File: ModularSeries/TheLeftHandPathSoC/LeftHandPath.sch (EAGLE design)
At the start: 64 parts, among them IC3 556_DUALTIMERDIL14, Q1 2N3906, Q2 2N3904, Q3 2N3904

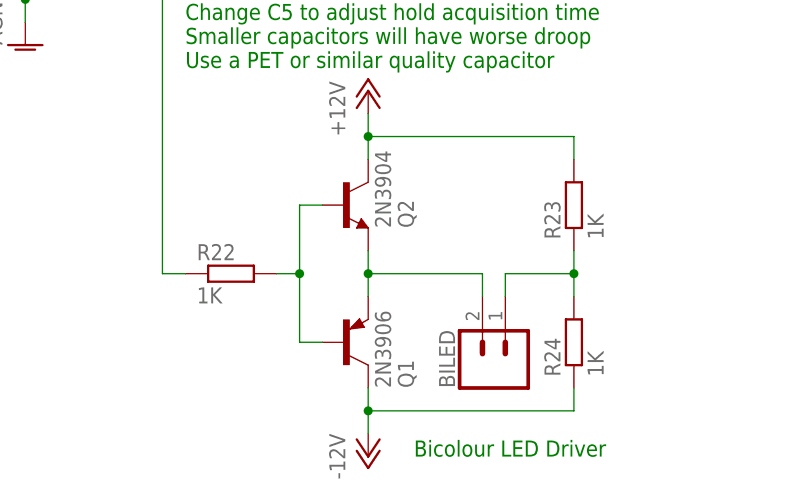
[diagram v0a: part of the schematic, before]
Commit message: Portals schematic renders brought up to date
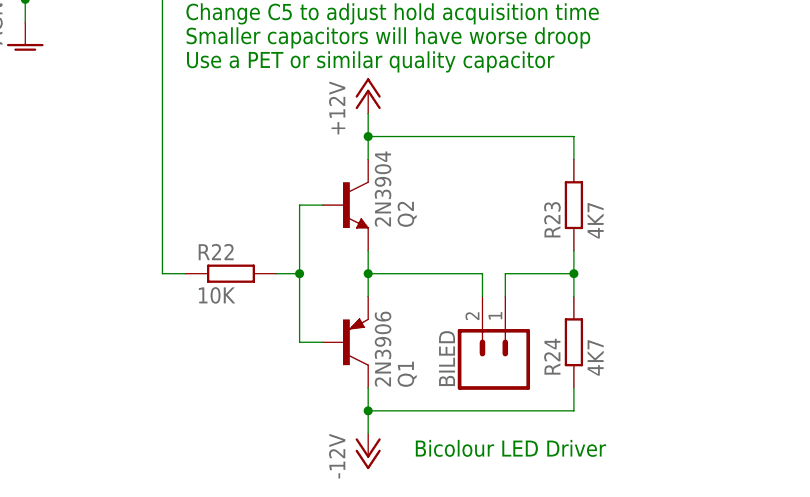
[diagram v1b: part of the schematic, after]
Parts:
- R22: value 1K -> 10K
- R23, R24: value 1K -> 4K7
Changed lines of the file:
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@@
 <part name="R21" library="rcl" library_urn="urn:adsk.eagle:library:334" deviceset="R-EU_" device="0207/7" package3d_urn="urn:adsk.eagle:package:23493/2" value="100Ω"/>
 <part name="WP1" library="ElectricNoodleBox" deviceset="COMBO_SUPPLY_HEADER" device=""/>
-<part name="R22" library="rcl" library_urn="urn:adsk.eagle:library:334" deviceset="R-EU_" device="0207/7" package3d_urn="urn:adsk.eagle:package:23493/2" value="1K"/>
+<part name="R22" library="rcl" library_urn="urn:adsk.eagle:library:334" deviceset="R-EU_" device="0207/7" package3d_urn="urn:adsk.eagle:package:23493/2" value="10K"/>
 <part name="Q2" library="transistor" library_urn="urn:adsk.eagle:library:402" deviceset="2N3904" device="" package3d_urn="urn:adsk.eagle:package:28523/2"/>
 <part name="Q1" library="transistor-pnp" library_urn="urn:adsk.eagle:library:399" deviceset="2N3906" device="" package3d_urn="urn:adsk.eagle:package:29211/2"/>
 <part name="P+4" library="supply1" library_urn="urn:adsk.eagle:library:371" deviceset="+12V" device=""/>
 <part name="P-3" library="supply1" library_urn="urn:adsk.eagle:library:371" deviceset="-12V" device=""/>
-<part name="R23" library="rcl" library_urn="urn:adsk.eagle:library:334" deviceset="R-EU_" device="0207/7" package3d_urn="urn:adsk.eagle:package:23493/2" value="1K"/>
-<part name="R24" library="rcl" library_urn="urn:adsk.eagle:library:334" deviceset="R-EU_" device="0207/7" package3d_urn="urn:adsk.eagle:package:23493/2" value="1K"/>
+<part name="R23" library="rcl" library_urn="urn:adsk.eagle:library:334" deviceset="R-EU_" device="0207/7" package3d_urn="urn:adsk.eagle:package:23493/2" value="4K7"/>
+<part name="R24" library="rcl" library_urn="urn:adsk.eagle:library:334" deviceset="R-EU_" device="0207/7" package3d_urn="urn:adsk.eagle:package:23493/2" value="4K7"/>
 <part name="BILED" library="ElectricNoodleBox" deviceset="2XWIREPAD" device=""/>
 </parts>

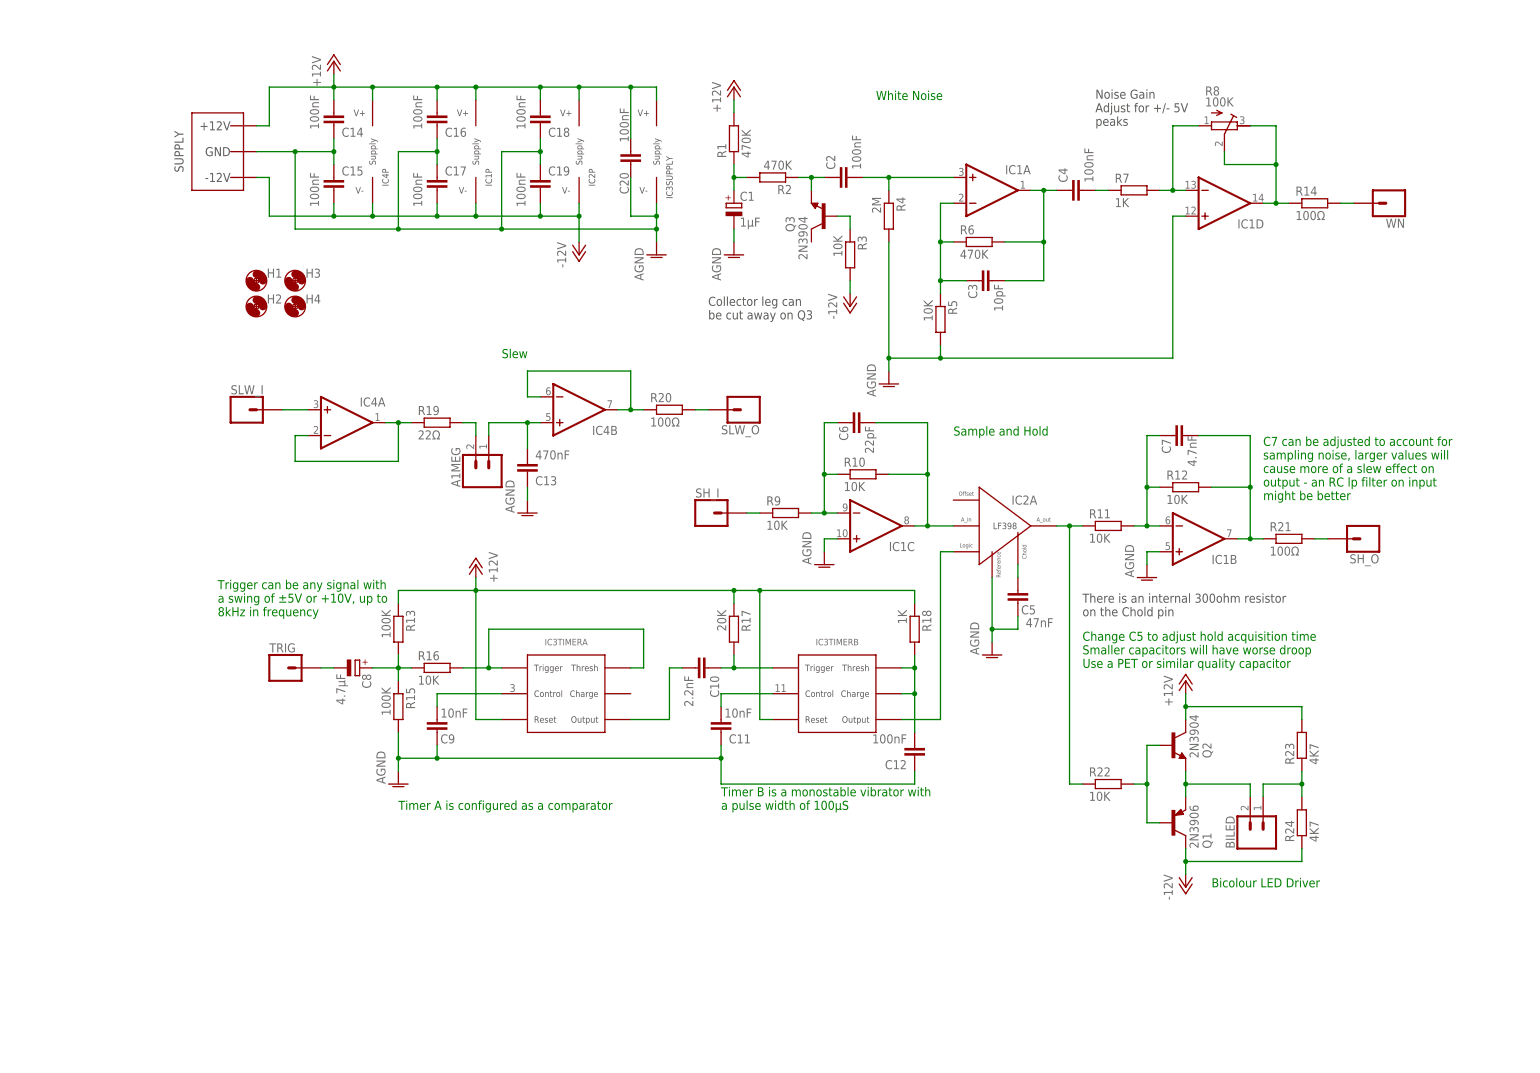
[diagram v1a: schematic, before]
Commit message: Left Hand Path Project added, Core, Control and Panel Cards
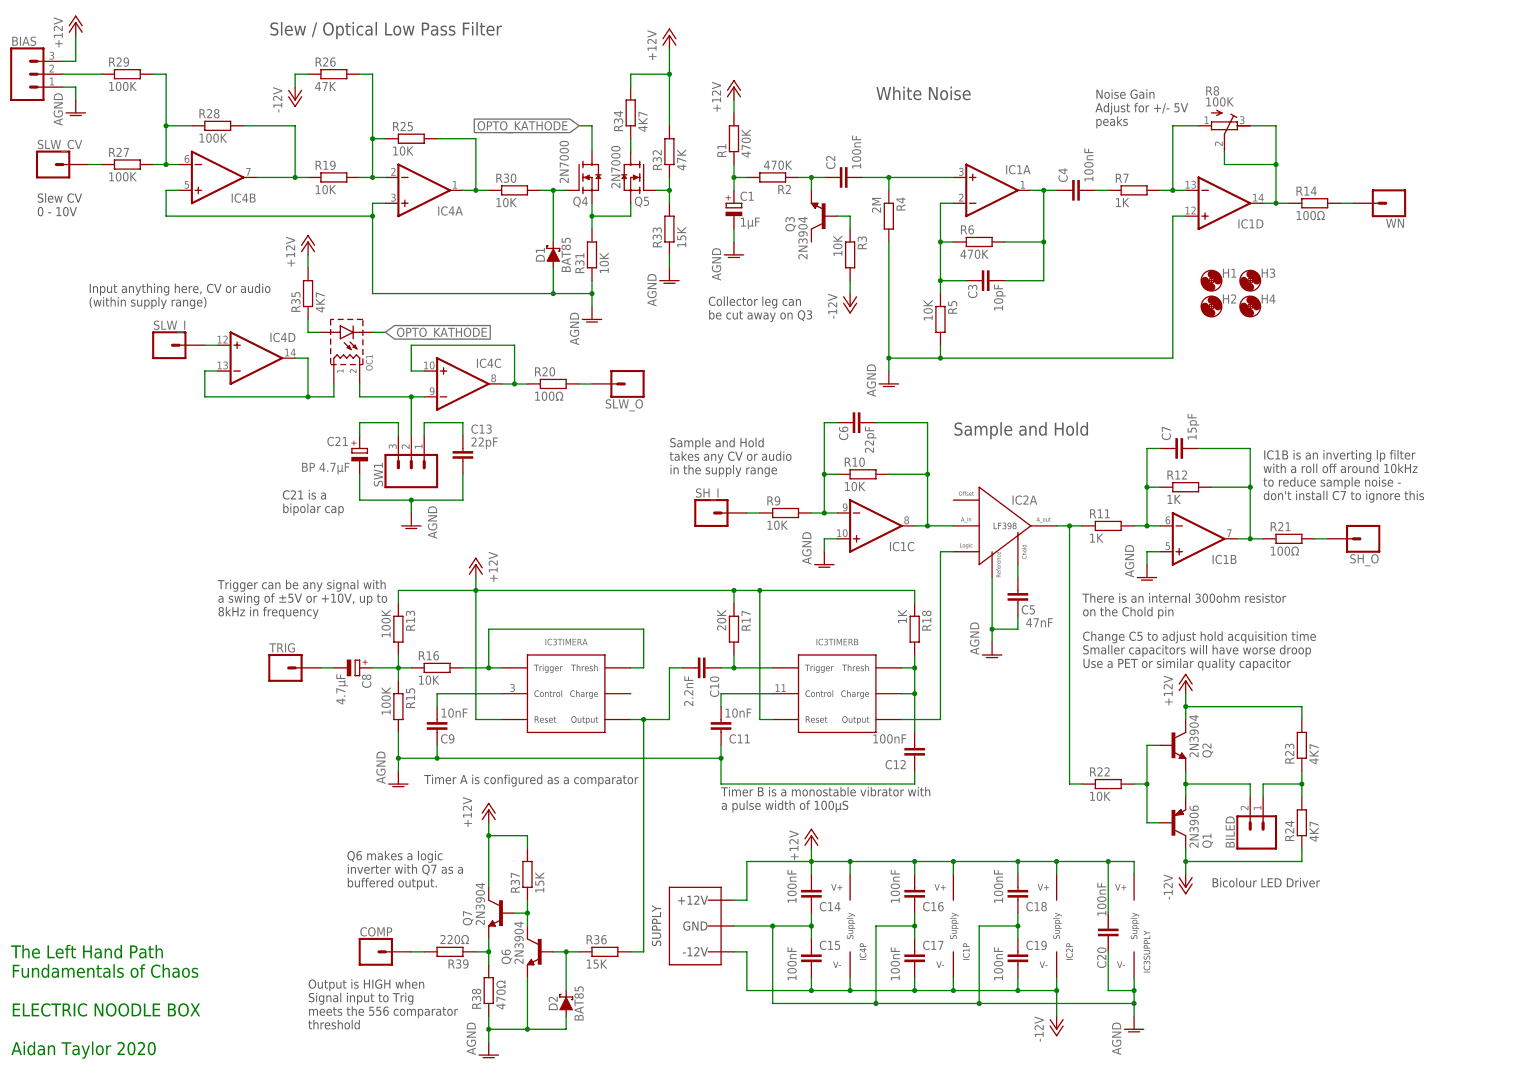
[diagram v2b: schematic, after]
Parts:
- removed A1MEG: 2XWIREPAD, ElectricNoodleBox:2XWIREPAD
- added BIAS, SW1: 3XWIREPAD, ElectricNoodleBox:3XWIREPAD
- added C21: BP 4.7µF, rcl:CPOL-EUE2-5
- added COMP, SLW_CV: 1XWIREPAD, ElectricNoodleBox:1XWIREPAD
- added D1, D2: BAT85, ElectricNoodleBox:SCHOTTKY_DO35
- added OC1: OPTOCOUPLERSILONEX, ElectricNoodleBox:OPTOCOUPLERSILONEX
- added Q4, Q5: 2N7000, ElectricNoodleBox:2N7000
- added Q6, Q7: 2N3904, transistor:2N3904
- added R25, R30, R31: 10K, rcl:R-EU_0207/7
- added R26, R32: 47K, rcl:R-EU_0207/7
- added R27, R28, R29: 100K, rcl:R-EU_0207/7
- added R33, R36, R37: 15K, rcl:R-EU_0207/7
- added R34, R35: 4K7, rcl:R-EU_0207/7
- added R38: 470Ω, rcl:R-EU_0207/7
- added R39: 220Ω, rcl:R-EU_0207/7
- C13: value 470nF -> 22pF
- C7: value 4.7nF -> 15pF
- IC4: device ElectricNoodleBox:TL0X2DIL -> ElectricNoodleBox:TL0X4DIL
- R11, R12: value 10K -> 1K
- R19: value 22Ω -> 10K
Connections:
- new net N$37: IC4A.-IN, R19.2, R25.1, R26.2
- new net N$38: IC4B.-IN, R27.2, R28.1, R29.2
- new net N$39: IC4A.OUT, R25.2, R30.1
- new net N$40: D1.C, Q4.G, R30.2
- new net N$41: Q4.S, Q5.S, R31.2
- new net N$42: C21.+, SW1.3
- new net N$43: Q5.G, R32.1, R33.2
- new net N$44: Q5.D, R34.1
- new net N$45: OC1.A, R35.1
- new net N$46: C13.2, SW1.1
- new net N$47: R27.1, SLW_CV.1
- new net N$48: BIAS.2, R29.1
- new net N$49: Q6.C, Q7.B, R37.1
- new net N$50: Q7.E, R38.2, R39.1
- new net N$51: COMP.1, R39.2
- new net N$52: D2.C, Q6.B, R36.1
- new net OPTO_KATHODE: OC1.K, Q4.D
- net +12V: now also BIAS.3, Q7.C, R32.2, R34.2, R35.2, R37.2
- net -12V: now also R26.1
- net AGND: now also BIAS.1, C21.-, D1.A, D2.A, IC4A.+IN, IC4B.+IN, Q6.E, R31.1, R33.1, R38.1
- net N$17: now also R36.2
- net N$27: now also IC4D.+IN; no longer IC4A.+IN
- net N$28: now also IC4D.-IN, IC4D.OUT, OC1.R1; no longer IC4A.-IN, IC4A.OUT, R19.1
- net N$29: now also IC4B.OUT, R19.1, R28.2; no longer A1MEG.2, R19.2
- net N$30: now also IC4C.-IN, OC1.R2, SW1.2; no longer A1MEG.1, C13.2, IC4B.+IN
- net N$31: now also IC4C.+IN, IC4C.OUT; no longer IC4B.-IN, IC4B.OUT
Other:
- note added: "C21 is a bipolar cap"
- note added: "IC1B is an inverting lp filter with a roll off around 10kHz to reduce sample noise - don't install C7 to ignore this"
- note added: "Input anything here, CV or audio (within supply range)"
- note added: "Output is HIGH when Signal input to Trig meets the 556 comparator threshold"
- note added: "Q6 makes a logic inverter with Q7 as a buffered output."
- note added: "Sample and Hold takes any CV or audio in the supply range"
- note added: "Slew / Optical Low Pass Filter"
- note added: "Slew CV 0 - 10V"
- note added: "The Left Hand Path Fundamentals of Chaos ELECTRIC NOODLE BOX Aidan Taylor 2020"
- note removed: "C7 can be adjusted to account for sampling noise, larger values will cause more of a slew effect on output - an RC lp filter on input might be better"
- note removed: "Slew"
- moved on the sheet: C13, C14, C15, C16, C17, C18, C19, C20, C7, H1, H2, H3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
